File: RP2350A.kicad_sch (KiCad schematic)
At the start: 40 parts, among them J14 USB_C_Receptacle_USB2.0_16P, J15 Conn_02x10_Counter_Clockwise, J16 Conn_ARM_SWD_TagConnect_TC203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, SW5 SW_Push, SW6 SW_Push, U35 ETA7014S2G, U36 RP2350A, U37 W25Q128JVS, Y6 TAXM12M4RLBDDT2T

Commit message: SBCv0.3
there is no big thing update just some LCSC & Mouser parts
and Big problem deleted alot of component values (:
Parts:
- removed C391, C392: 34pF, Capacitor_SMD:C_0402_1005Metric_Pad0.74x0.62mm_HandSolder, symbol New_Library_0:C_Small_edited
- added C352, C354: 34pF, Capacitor_SMD:C_0402_1005Metric_Pad0.74x0.62mm_HandSolder, symbol New_Library_0:C_Small_edited
- C376, C378, C379, C380, C381, C382, C383, C384, C385, C386, C387, C388: footprint Capacitor_SMD:C_0402_1005Metric_Pad0.74x0.62mm_HandSolder -> Capacitor_SMD:C_0201_0603Metric_Pad0.64x0.40mm_HandSolder; LCSC Part (none) -> C5209398; Mouser Part (none) -> CL03A105KP3NSNC
- C377: LCSC Part (none) -> C86295; Mouser Part (none) -> CL10A226MP8NUNE
- C389, C390, C393: LCSC Part (none) -> C5209398; Mouser Part (none) -> CL03A105KP3NSNC
- D22: LCSC Part (none) -> C113975; Mouser Part (none) -> 581-SMBJ5.0CA
- J14: value USB_C_Receptacle_USB2.0_16P -> GT-USB-7010ASV; footprint (none) -> Connector_USB:USB_C_Receptacle_G-Switch_GT-USB-7010ASV; LCSC Part (none) -> C2988369
- J15: value Conn_02x10_Counter_Clockwise -> B-2100S20P-B110; LCSC Part (none) -> C124359
- J16: value Conn_ARM_SWD_TagConnect_TC2030-NL -> JTag Connector; now not fitted
- L15: LCSC Part (none) -> (hide yes)
- R177: value 100k -> (none); LCSC Part (none) -> (show_name no)
- R178, R184: value 10k -> (none); LCSC Part (none) -> (at 0 0 0)
- R179: value 4.7k -> (none); LCSC Part (none) -> (show_name no)
- R180, R181: value 5.1k -> )
- R182: value 5.1k -> (symbol "C_Small_edited_0_1"
- R183, R186: value 0R -> (none); LCSC Part (none) -> )
- R185: value 1k -> (none); LCSC Part (none) -> (show_name no)
- R187: value 1k -> (none); LCSC Part (none) -> (effects
- SW5, SW6: value SW_Push -> (none); Mouser Part (none) -> (pts
- U35: value ETA7014S2G -> (none); Mouser Part (none) -> (pts
- U36: value RP2350A -> AP2553W6-7; footprint Package_DFN_QFN:QFN-60-1EP_7x7mm_P0.4mm_EP3.4x3.4mm -> Package_TO_SOT_SMD:SOT-23-6_Handsoldering; LCSC Part (none) -> C212302; Mouser Part (none) -> 621-AP2553W6-7
- U37: value W25Q128JVS -> (none); footprint Package_SO:SOIC-8_5.3x5.3mm_P1.27mm -> )
- Y6: value TAXM12M4RLBDDT2T -> (none); LCSC Part (none) -> )
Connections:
- net Crystal_{MCU}_IN: now also C352.1
- net Crystal_{MCU}_OUT: now also C354.1
- net GND: now also C352.2, C354.2

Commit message: SBCv0.4
add LCSC & Mouser parts 
and solve the deleted value in the past version
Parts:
- removed R183: (no value), PCM_Resistor_SMD_AKL:R_0402_1005Metric_Pad0.72x0.64mm, symbol Device:R_Small
- L15: value YL201209-3R3K -> 3.3uH; LCSC Part (hide yes) -> C2926398
- R177: value (none) -> 100k; LCSC Part (show_name no) -> C60491; Mouser Part (none) -> 603-RC0402FR-07100KL
- R178, R184: value (none) -> 10k; LCSC Part (at 0 0 0) -> C60490; Mouser Part (none) -> 603-RC0402FR-0710KL
- R179: value (none) -> 4.7k; LCSC Part (show_name no) -> C105871; Mouser Part (none) -> 603-RC0402FR-074K7L
- R180, R181: value ) -> 5.1k; footprint PCM_Resistor_SMD_AKL:R_0402_1005Metric_Pad0.72x0.64mm -> PCM_Resistor_SMD_AKL:R_0402_1005Metric; LCSC Part (none) -> C105872; Mouser Part (none) -> 603-RC0402FR-075K1L
- R182: value (symbol "C_Small_edited_0_1" -> 5.1k; LCSC Part (none) -> C105872; Mouser Part (none) -> 603-RC0402FR-075K1L
- R185: value (none) -> 1k; footprint PCM_Resistor_SMD_AKL:R_0402_1005Metric_Pad0.72x0.64mm -> PCM_Resistor_SMD_AKL:R_0402_1005Metric; LCSC Part (show_name no) -> C106235; Mouser Part (none) -> 603-RC0402FR-071KL
- R186: value (none) -> 0R; footprint PCM_Resistor_SMD_AKL:R_0402_1005Metric_Pad0.72x0.64mm -> PCM_Resistor_SMD_AKL:R_0402_1005Metric; LCSC Part ) -> C106231; Mouser Part (none) -> 603-RC0402FR-070RL
- R187: value (none) -> 1k; LCSC Part (effects -> C106235; Mouser Part (none) -> 603-RC0402FR-071KL
- SW5, SW6: value (none) -> XUNPU TS-1089S-02526; footprint Button_Switch_SMD:SW_Push_1P1T_NO_CK_PTS125Sx85SMTR -> easyeda2kicad:XUNPU TS-1089S-02526; LCSC Part (none) -> C455282; Mouser Part (pts -> (none)
- U35: value (none) -> ETA7014S2G; LCSC Part (none) -> C7465500; Mouser Part (pts -> (none)
- U37: value (none) -> W25Q128JVS; footprint ) -> Package_SO:SOIC-8_5.3x5.3mm_P1.27mm; LCSC Part (none) -> C97521; Mouser Part (none) -> 454-W25Q128JVSIQTR
- Y6: value (none) -> TAXM12M4RLBDDT2T; LCSC Part ) -> C133334

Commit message: Release v2: replace main with RK3576 SBCv2, archive v1 to branch archive/v1
- main now shows only v2 (RK3576 SBCv2.kicad_pro)
- v1 preserved in branch archive/v1 + tag v1.0
- Add .gitignore for KiCad (*.bak, *.lck, .history/)
- Update README with version switcher
- Cleaned: dropped 141M .history, Resources ref PDF, *.bak/*.lck
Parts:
- removed C354: 34pF, Capacitor_SMD:C_0402_1005Metric_Pad0.74x0.62mm_HandSolder, symbol New_Library_0:C_Small_edited
- removed C376, C378, C379, C380, C381: 1u, Capacitor_SMD:C_0201_0603Metric_Pad0.64x0.40mm_HandSolder, symbol New_Library_0:C_Small_edited
- removed C377: 22u, Capacitor_SMD:C_0603_1608Metric, symbol New_Library_0:C_Small_edited
- removed D22: SMBJ5.0CA, PCM_Diode_SMD_AKL:D_SMB_TVS, symbol PCM_Diode_TVS_AKL:SMBJ5.0CA
- removed J14: GT-USB-7010ASV, Connector_USB:USB_C_Receptacle_G-Switch_GT-USB-7010ASV, symbol Connector:USB_C_Receptacle_USB2.0_16P
- removed J15: B-2100S20P-B110, Connector_PinHeader_2.54mm:PinHeader_2x10_P2.54mm_Vertical_SMD, symbol Connector_Generic:Conn_02x10_Counter_Clockwise
- removed J16: JTag Connector, Connector:Tag-Connect_TC2030-IDC-NL_2x03_P1.27mm_Vertical, symbol Connector:Conn_ARM_SWD_TagConnect_TC2030-NL
- removed L15: 3.3uH, Inductor_SMD:L_Coilcraft_0805HQ_2012Metric, symbol Device:L_Small
- removed R177: 100k, PCM_Resistor_SMD_AKL:R_0402_1005Metric, symbol Device:R_Small
- removed R178, R184: 10k, PCM_Resistor_SMD_AKL:R_0402_1005Metric, symbol Device:R_Small
- removed R179: 4.7k, PCM_Resistor_SMD_AKL:R_0402_1005Metric, symbol Device:R_Small
- removed R180, R181, R182: 5.1k, PCM_Resistor_SMD_AKL:R_0402_1005Metric, symbol Device:R_Small
- removed R185, R187: 1k, PCM_Resistor_SMD_AKL:R_0402_1005Metric, symbol Device:R_Small
- removed R186: 0R, PCM_Resistor_SMD_AKL:R_0402_1005Metric, symbol Device:R_Small
- removed Y6: TAXM12M4RLBDDT2T, Crystal:Crystal_SMD_3225-4Pin_3.2x2.5mm_HandSoldering, symbol Device:Crystal_GND24
- added C355: 34pF, Capacitor_SMD:C_0402_1005Metric_Pad0.74x0.62mm_HandSolder, symbol New_Library_0:C_Small_edited
- added C391, C392, C398, C410, C411, C412: 1u, Capacitor_SMD:C_0201_0603Metric_Pad0.64x0.40mm_HandSolder, symbol New_Library_0:C_Small_edited
- added D26: SMBJ5.0CA, PCM_Diode_SMD_AKL:D_SMB_TVS, symbol PCM_Diode_TVS_AKL:SMBJ5.0CA
- added J18: TYPEC-305-ACP16H458, Datasheet_Footprints:USB-C-SMD-16P_TYPEC-305-ACP16H458, symbol Connector:USB_C_Receptacle_USB2.0_16P
- added J19: JTag Connector, Connector:Tag-Connect_TC2030-IDC-NL_2x03_P1.27mm_Vertical, symbol Connector:Conn_ARM_SWD_TagConnect_TC2030-NL
- added J20: B-2100S20P-B110, Connector_PinHeader_2.54mm:PinHeader_2x10_P2.54mm_Vertical_SMD, symbol Connector_Generic:Conn_02x10_Counter_Clockwise
- added L16: 3.3uH, Inductor_SMD:L_Coilcraft_0805HQ_2012Metric, symbol Device:L_Small
- added R144, R209: 0R, PCM_Resistor_SMD_AKL:R_0402_1005Metric, symbol Device:R_Small
- added R188, R204, R212: 5.1k, PCM_Resistor_SMD_AKL:R_0402_1005Metric, symbol Device:R_Small
- added R205: 100k, PCM_Resistor_SMD_AKL:R_0402_1005Metric, symbol Device:R_Small
- added R206, R211: 10k, PCM_Resistor_SMD_AKL:R_0402_1005Metric, symbol Device:R_Small
- added R207: 4.7k, PCM_Resistor_SMD_AKL:R_0402_1005Metric, symbol Device:R_Small
- added R208, R210: 1k, PCM_Resistor_SMD_AKL:R_0402_1005Metric, symbol Device:R_Small
- added Y7: TAXM12M4RLBDDT2T, Crystal:Crystal_SMD_3225-4Pin_3.2x2.5mm_HandSoldering, symbol Device:Crystal_GND24
- C382: value 1u -> 22u; footprint Capacitor_SMD:C_0201_0603Metric_Pad0.64x0.40mm_HandSolder -> Capacitor_SMD:C_0603_1608Metric; LCSC Part C5209398 -> C86295; Mouser Part CL03A105KP3NSNC -> CL10A226MP8NUNE
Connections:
- net ADC0_{MCU}: now also J20.15 (Pin_15)
- net ADC1_{MCU}: now also J20.16 (Pin_16)
- net ADC2_{MCU}: now also J20.17 (Pin_17)
- net ADC3_{MCU}: now also J20.18 (Pin_18)
- net Crystal_{MCU}_IN: now also Y7.1
- net Crystal_{MCU}_OUT: now also C355.1, Y7.3
- net Flash_{MCU}_SS: now also R209.2
- net GND: now also C355.2, C391.2, C392.2, C398.2, C410.2, C411.2, C412.2, D26.1 (K), J18.A1 (GND), J18.A12 (GND), J18.B1 (GND), J18.B12 (GND), J19.5 (GND), J20.19 (Pin_19), J20.20 (Pin_20), R144.2, R188.2, R204.2, R207.2, Y7.2 (G), Y7.4 (G)
- net GPIO_{MCU}_22: now also J20.11 (Pin_11)
- net GPIO_{MCU}_23: now also J20.12 (Pin_12)
- net GPIO_{MCU}_24: now also J20.13 (Pin_13)
- net GPIO_{MCU}_25: now also J20.14 (Pin_14)
- net GPIO_{MCU}_6: now also J20.7 (Pin_7)
- net GPIO_{MCU}_7: now also J20.8 (Pin_8)
- net I2C0_{MCU}_SCL: now also J20.6 (Pin_6)
- net I2C0_{MCU}_SDA: now also J20.5 (Pin_5)
- net Reset_{MCU}: now also J19.3 (~{RESET}), R210.2, R211.2
- net SWCLK_{MCU}: now also J19.4 (SWCLK)
- net SWDIO_{MCU}: now also J19.2 (SWDIO)
- net UART1_{MCU}_RX: now also J20.10 (Pin_10)
- net UART1_{MCU}_TX: now also J20.9 (Pin_9)
- net USB_{MCU}_N: now also J18.A7 (D-), J18.B7 (D-)
- net USB_{MCU}_P: now also J18.A6 (D+), J18.B6 (D+)
- net VCC5V0_SYS: now also J20.1 (Pin_1), J20.2 (Pin_2)
- net VCC_3V3_S0: now also C391.1, C392.1, C398.1, C410.1, C411.1, C412.1, J19.1 (VCC), J20.3 (Pin_3), J20.4 (Pin_4), R211.1, R212.1; no longer C382.1, C383.1, C384.1, C385.1, C386.1, C387.1
- net Vbus_USB_{MCU}: now also C384.1, R206.1
- net Vdet_USB_{MCU}: now also R206.2, R207.1
- net at U35.2 (EN), U35.4 (IN): now also C382.1, D26.2 (A), J18.A4 (VBUS), J18.A9 (VBUS), J18.B4 (VBUS), J18.B9 (VBUS), R205.1
- net at U35.5 (VCC): now also C383.1, R205.2
- net at C389.1, U36.46 (VREG_AVDD): now also R212.2
- net at SW6.2: now also R208.2
- net at SW5.2: now also R210.1
- net at U37.1 (~{CS}): now also R208.1, R209.1
- net at U36.48 (VREG_LX): now also L16.2
- net 1.1v renamed VCC_1V1_S0
- net VCC_1V1_S0: now also C385.1, C386.1, C387.1, L16.1
- new net: J18.A5 (CC1), R188.1
- new net: J18.B5 (CC2), R204.1
- new net: J18.SH (SHIELD), R144.1

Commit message: Replace v2 with updated RK3576_SBCv2 (Copy) Oct 2
- Update 18 sheets to Oct 2 15:37 local versions
- Keep cleaned layout: exclude .history/, Resources/, *.bak, *.lck,
  project.kicad_dru, .hs_rules.json, lowercase dup placeholders
  (fixtures/power), empty orphans (digital, mechanical, output,
  USBC_MCU, eMMC_UFS)
- Preserve LICENSE, README.md, .gitignore
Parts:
- C352, C355: footprint Capacitor_SMD:C_0402_1005Metric_Pad0.74x0.62mm_HandSolder -> Capacitor_SMD:C_0402_1005Metric
- R205: LCSC Part C60491 -> C60490; Mouser Part 603-RC0402FR-07100KL -> 603-RC0402FR-0710KL
- U36: value AP2553W6-7 -> RP2350A; footprint Package_TO_SOT_SMD:SOT-23-6_Handsoldering -> Package_DFN_QFN:QFN-60-1EP_7x7mm_P0.4mm_EP3.4x3.4mm; LCSC Part C212302 -> C42411118; Mouser Part 621-AP2553W6-7 -> 358-SC150913

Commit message: Relink hierarchical root: 18 sheets into RK3576 SBCv2 top level
Root was empty (no sheet boxes); all subsheets orphaned.
Rebuilt A1 top level linking RK3576, LPDDR5, Power, Ethernet,
HDMI, MIPI, PCIe, USB-A/C, Wireless, RTC, uSD, GPIO, OLED,
RP2350A, Connectors, Fixtures, DC_Power. block_diagrame kept
docs-only (unlinked, avoids double-instantiation). Lowercase
stub duplicates excluded. ERC: 1388 -> 770 violations.
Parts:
- removed J18: TYPEC-305-ACP16H458, Datasheet_Footprints:USB-C-SMD-16P_TYPEC-305-ACP16H458, symbol Connector:USB_C_Receptacle_USB2.0_16P
- added J2: TYPEC-305-ACP16H458, Datasheet_Footprints:USB-C-SMD_TYPEC-305-ACP16H458, symbol Connector:USB_C_Receptacle_USB2.0_16P
- renumbered C382 to C113, C383 to C114, C390 to C115, C384 to C116, C393 to C117, C352 to C118, C355 to C119, C385 to C120, C389 to C121, C386 to C122, C387 to C123, C388 to C124, C391 to C125, C392 to C126, C398 to C127, C410 to C128, C411 to C129, C412 to C130, D26 to D4, J19 to J3, J20 to J4, L16 to L1, R144 to R36, R188 to R37, R204 to R38, R205 to R39, R206 to R40, R207 to R41, R208 to R42, R209 to R43, R210 to R44, R211 to R45, R212 to R46, SW6 to SW3, SW5 to SW4, U37 to U2, U35 to U3, U36 to U4, Y7 to Y3
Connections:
- net GND: now also J2.A1 (GND), J2.A12 (GND), J2.B1 (GND), J2.B12 (GND)
- net USB_{MCU}_N: now also J2.A7 (D-), J2.B7 (D-)
- net USB_{MCU}_P: now also J2.A6 (D+), J2.B6 (D+)
- net at C113.1, D4.2 (A), R39.1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: now also J2.A4 (VBUS), J2.A9 (VBUS), J2.B4 (VBUS), J2.B9 (VBUS)
- net at R37.1: now also J2.A5 (CC1)
- net at R38.1: now also J2.B5 (CC2)
- net at R36.1: now also J2.SH (SHIELD)

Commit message: Update v2 schematics + PCB: impedance profiles, design rules, sheet fixes
- pro: copper/track widths, microvias, 40/50 OHM + DIFF 85/90/100 tuning profiles
- dru/pcb: updated constraints and layout
- sheets: RK3576, RP2350A, Fixtures, MIPI, PCIe, HDMI, LPDDR5, UFS/eMMC, OLED, block diagram
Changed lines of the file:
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@@
 		(at 167.64 231.14)
 	)
+	(bus_entry
+		(at 274.32 165.1)
+		(size 2.54 -2.54)
+		(stroke
+			(width 0)
+			(type default)
+		)
+	)
+	(bus_entry
+		(at 274.32 157.48)
+		(size 2.54 -2.54)
+		(stroke
+			(width 0)
+			(type default)
+		)
+	)
+	(bus_entry
+		(at 274.32 162.56)
+		(size 2.54 -2.54)
+		(stroke
+			(width 0)
+			(type default)
+		)
+	)
+	(bus_entry
+		(at 274.32 154.94)
+		(size 2.54 -2.54)
+		(stroke
+			(width 0)
+			(type default)
+		)
+	)
+	(bus_entry
+		(at 274.32 160.02)
+		(size 2.54 -2.54)
+		(stroke
+			(width 0)
+			(type default)
+		)
+	)
 	(wire
 		(pts
@@
 		)
 	)
+	(bus
+		(pts
+			(xy 276.86 152.4) (xy 276.86 162.56)
+		)
+		(stroke
+			(width 0)
+			(type default)
+		)
+	)
 	(wire
 		(pts
@@
 		)
 	)
+	(bus
+		(pts
+			(xy 276.86 152.4) (xy 278.13 152.4)
+		)
+		(stroke
+			(width 0)
+			(type default)
+		)
+	)
 	(wire
 		(pts
@@
 		)
 	)
+	(hierarchical_label "OLED Display"
+		(shape bidirectional)
+		(at 278.13 152.4 0)
+		(effects
+			(font
+				(size 1.27 1.27)
+			)
+			(justify left)
+		)
+	)

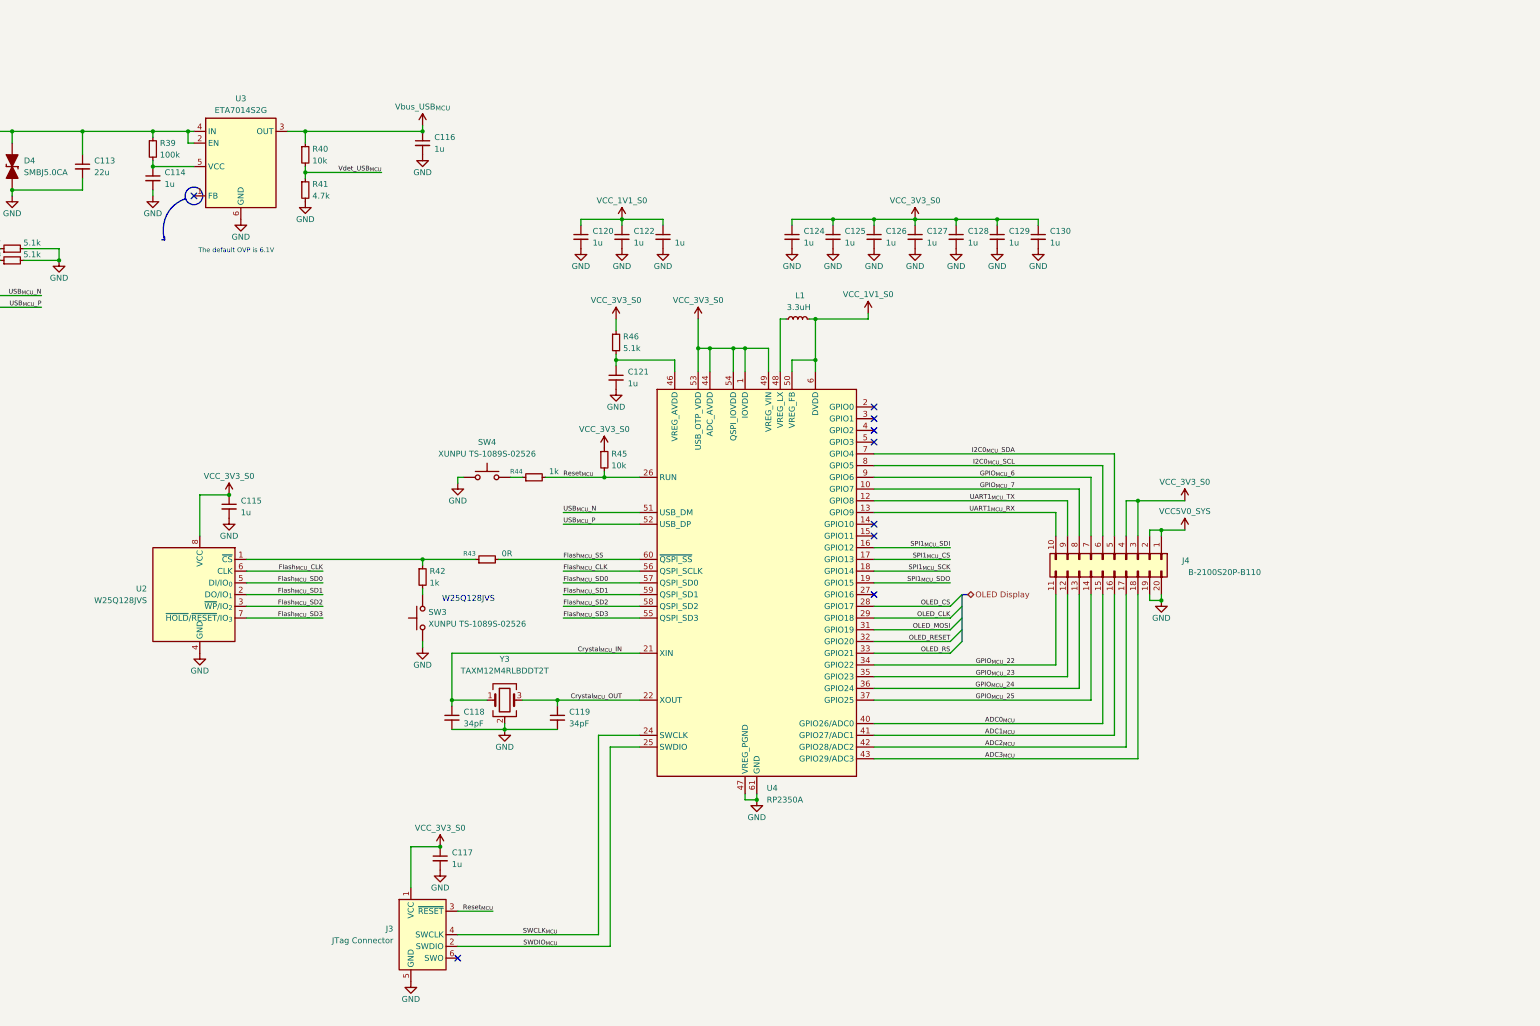
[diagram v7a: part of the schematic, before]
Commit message: block diagrame with Hierarchical labels and NVMe SSD footprint
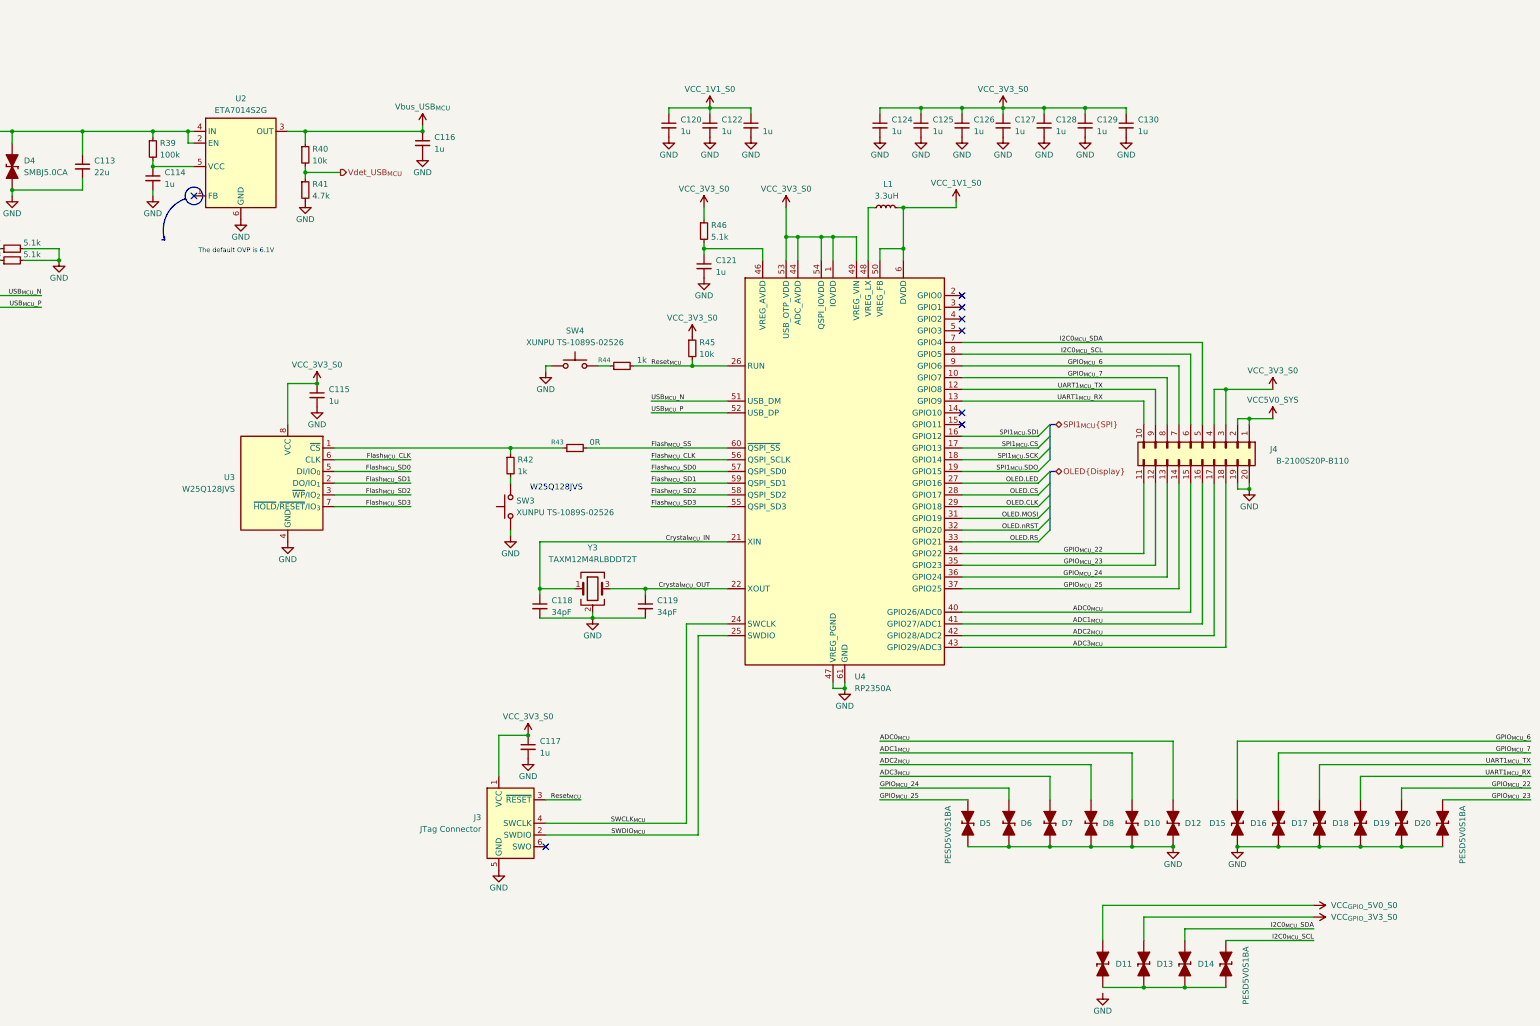
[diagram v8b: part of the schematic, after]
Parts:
- added D10, D11, D12, D13, D14, D15, D16, D17, D18, D19, D20, D5, D6, D7, D8, D9: PESD5V0S1BA, PCM_Diode_SMD_AKL:D_SOD-323_TVS, symbol PCM_Diode_TVS_AKL:PESD5V0S1BA
- J4: footprint Connector_PinHeader_2.54mm:PinHeader_2x10_P2.54mm_Vertical_SMD -> Connector_PinSocket_2.54mm:PinSocket_2x10_P2.54mm_Horizontal
- renumbered U3 to U2, U2 to U3
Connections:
- net ADC0_{MCU}: now also D12.2 (A)
- net ADC1_{MCU}: now also D10.2 (A)
- net ADC2_{MCU}: now also D8.2 (A)
- net ADC3_{MCU}: now also D7.2 (A)
- net GND: now also D10.1 (K), D12.1 (K), D15.1 (K), D16.1 (K), D17.1 (K), D18.1 (K), D19.1 (K), D20.1 (K), D5.1 (K), D6.1 (K), D7.1 (K), D8.1 (K)
- net GPIO_{MCU}_22: now also D19.2 (A)
- net GPIO_{MCU}_23: now also D20.2 (A)
- net GPIO_{MCU}_24: now also D6.2 (A)
- net GPIO_{MCU}_25: now also D5.2 (A)
- net GPIO_{MCU}_6: now also D15.2 (A)
- net GPIO_{MCU}_7: now also D16.2 (A)
- net I2C0_{MCU}_SCL: now also D14.2 (A)
- net I2C0_{MCU}_SDA: now also D13.2 (A)
- net UART1_{MCU}_RX: now also D18.2 (A)
- net UART1_{MCU}_TX: now also D17.2 (A)
- net OLED.LED: now reaches U4.27 (GPIO16)
- net OLED_CLK renamed OLED.CLK
- net OLED_CS renamed OLED.CS
- net OLED_MOSI renamed OLED.MOSI
- net OLED_RESET renamed OLED.nRST
- net OLED_RS renamed OLED.RS
- net SPI1_{MCU}_CS renamed SPI1_{MCU}.CS
- net SPI1_{MCU}_SCK renamed SPI1_{MCU}.SCK
- net SPI1_{MCU}_SDI renamed SPI1_{MCU}.SDI
- net SPI1_{MCU}_SDO renamed SPI1_{MCU}.SDO
- new net: D11.1 (K), D13.1 (K), D14.1 (K), D9.1 (K)
- new net VCC_{GPIO}_3V3_S0: D11.2 (A)
- new net VCC_{GPIO}_5V0_S0: D9.2 (A)
- no-connect marks 11 -> 10
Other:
- moved on the sheet: C115, C117, C118, C119, C120, C121, C122, C124, C125, C126, C127, C128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
